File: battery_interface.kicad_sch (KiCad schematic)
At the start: 19 parts, among them J1 Conn_01x09

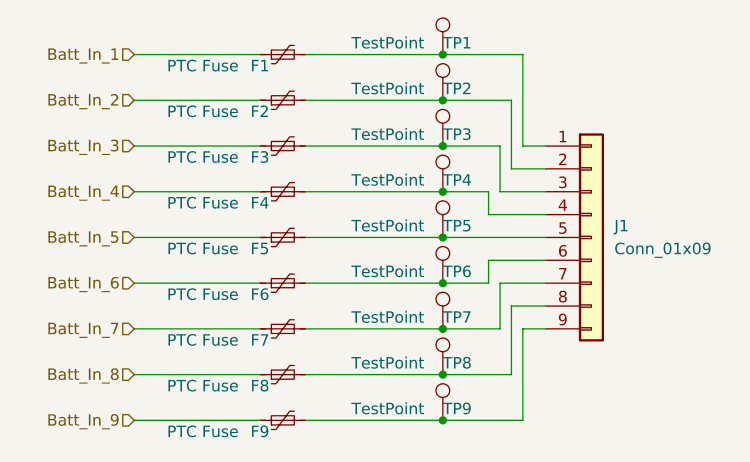
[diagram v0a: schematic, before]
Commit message: fixed spacing and schematic
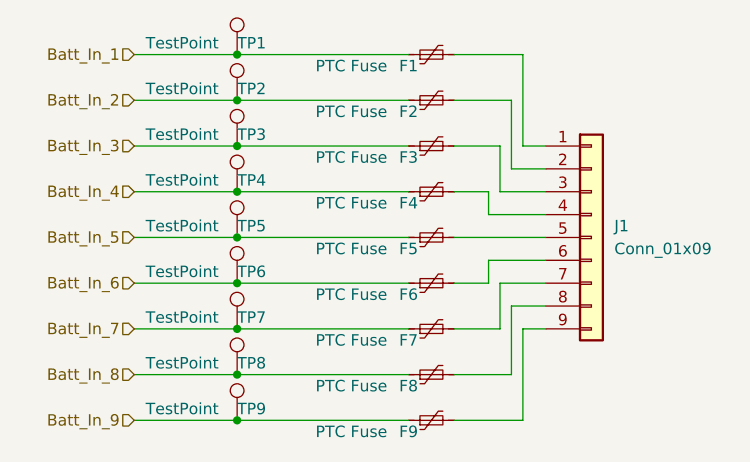
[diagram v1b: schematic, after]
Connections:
- net Batt_In_1: now also TP1.1
- net Batt_In_2: now also TP2.1
- net Batt_In_3: now also TP3.1
- net Batt_In_4: now also TP4.1
- net Batt_In_5: now also TP5.1
- net Batt_In_6: now also TP6.1
- net Batt_In_7: now also TP7.1
- net Batt_In_8: now also TP8.1
- net Batt_In_9: now also TP9.1
- net at F6.2, J1.6 (Pin_6): no longer TP6.1
- net at F4.2, J1.4 (Pin_4): no longer TP4.1
- net at F1.2, J1.1 (Pin_1): no longer TP1.1
- net at F2.2, J1.2 (Pin_2): no longer TP2.1
- net at F3.2, J1.3 (Pin_3): no longer TP3.1
- net at F5.2, J1.5 (Pin_5): no longer TP5.1
- net at F7.2, J1.7 (Pin_7): no longer TP7.1
- net at F8.2, J1.8 (Pin_8): no longer TP8.1
- net at F9.2, J1.9 (Pin_9): no longer TP9.1
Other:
- moved on the sheet: F1, F2, F3, F4, F5, F6, F7, F8, F9, TP1, TP2, TP3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
